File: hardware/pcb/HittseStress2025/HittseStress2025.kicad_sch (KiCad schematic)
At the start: 10 parts, among them J1 Conn_01x02_Socket, J2 Conn_01x02_Socket, J3 SMA_conector_female, U1 MINIDCDCBOOST5V, U2 TTGO_T-Beam_T22_V1.1

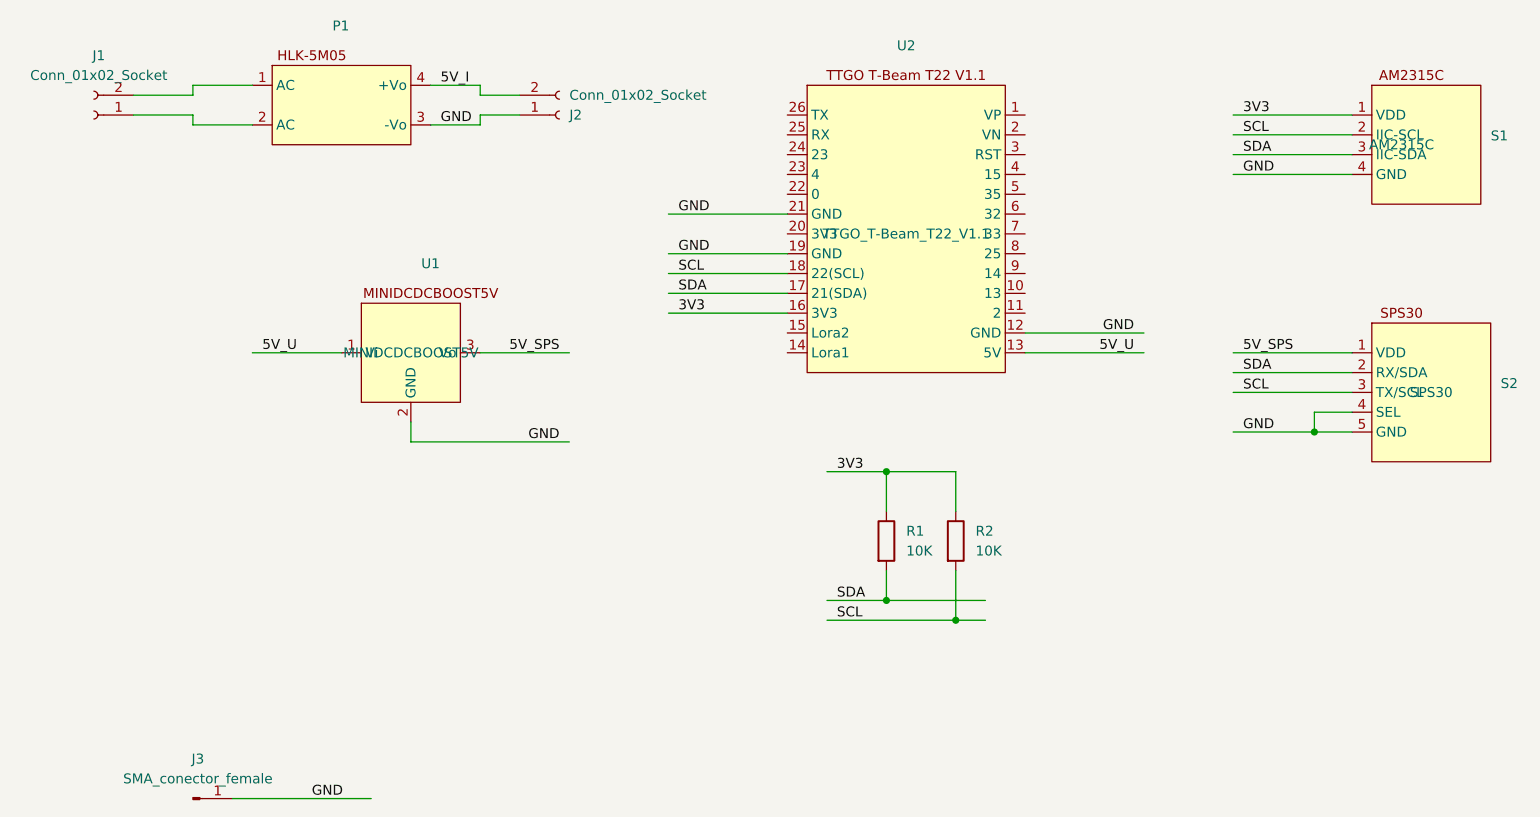
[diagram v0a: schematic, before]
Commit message: Updated to version 2025 for use with LilyGO T-Beam V1.2
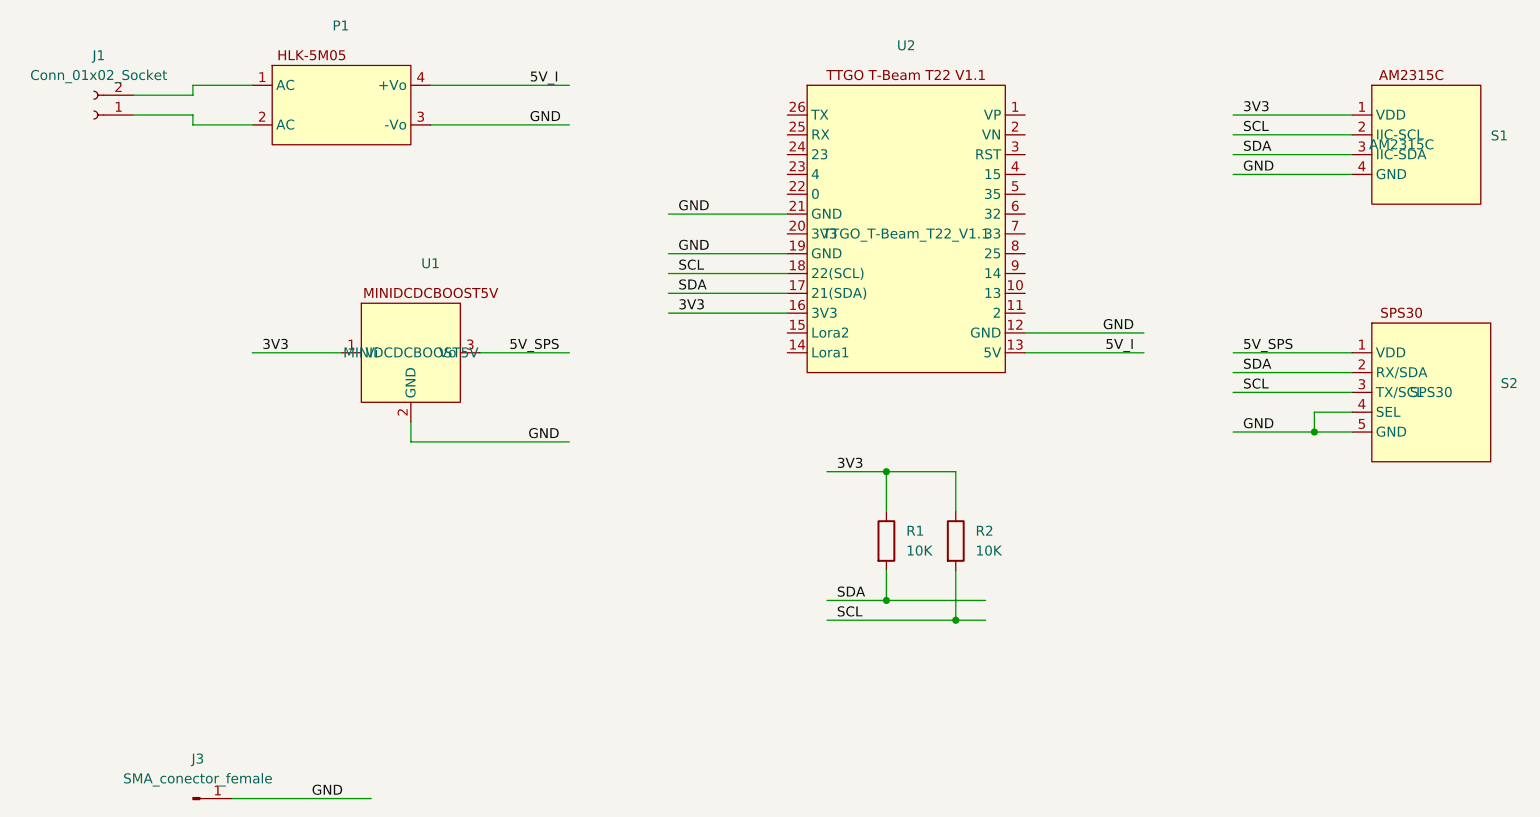
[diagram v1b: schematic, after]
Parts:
- removed J2: Conn_01x02_Socket, TerminalBlock_Phoenix:TerminalBlock_Phoenix_MPT-0,5-2-2.54_1x02_P2.54mm_Horizontal, symbol Connector:Conn_01x02_Socket
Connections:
- net 3V3: now also U1.1 (Vi)
- net 5V_I: now also U2.13 (5V)
- removed net 5V_U: U1.1 (Vi), U2.13 (5V)
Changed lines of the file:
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@@
-	(wire
-		(pts
-			(xy 81.28 64.77) (xy 81.28 66.04)
-		)
-		(stroke
-			(width 0)
-			(type default)
-		)
-	)
 	(wire
 		(pts
@@
 	(wire
 		(pts
-			(xy 81.28 60.96) (xy 81.28 62.23)
-		)
-		(stroke
-			(width 0)
-			(type default)
-		)
-	)
-	(wire
-		(pts
 			(xy 44.45 66.04) (xy 44.45 64.77)
 		)
@@
 	(wire
 		(pts
-			(xy 86.36 64.77) (xy 81.28 64.77)
-		)
-		(stroke
-			(width 0)
-			(type default)
-		)
-	)
-	(wire
-		(pts
 			(xy 125.73 129.54) (xy 142.24 129.54)
 		)
@@
 	(wire
 		(pts
-			(xy 81.28 62.23) (xy 86.36 62.23)
-		)
-		(stroke
-			(width 0)
-			(type default)
-		)
-	)
-	(wire
-		(pts
 			(xy 177.8 72.39) (xy 193.04 72.39)
 		)
@@
 	(wire
 		(pts
-			(xy 74.93 60.96) (xy 81.28 60.96)
+			(xy 74.93 60.96) (xy 92.71 60.96)
 		)
 		(stroke
@@
 	(wire
 		(pts
-			(xy 81.28 66.04) (xy 74.93 66.04)
-		)
-		(stroke
-			(width 0)
-			(type default)
-		)
-	)
-	(label "5V_U"
+			(xy 74.93 66.04) (xy 92.71 66.04)
+		)
+		(stroke
+			(width 0)
+			(type default)
+		)
+	)
+	(label "5V_I"
 		(at 165.1 95.25 180)
 		(effects
@@
 		)
 	)
-	(label "5V_U"
+	(label "3V3"
 		(at 53.34 95.25 0)
 		(effects
@@
 	)
 	(label "GND"
-		(at 76.2 66.04 0)
+		(at 87.63 66.04 0)
 		(effects
 			(font
@@
 	)
 	(label "5V_I"
-		(at 76.2 60.96 0)
+		(at 87.63 60.96 0)
 		(effects
 			(font
@@
 					(unit 1)
 				)
-			)
-		)
-	)
-	(symbol
-		(lib_id "Connector:Conn_01x02_Socket")
-		(at 91.44 64.77 0)
-		(mirror x)
-		(unit 1)
-		(exclude_from_sim no)
-		(in_bom yes)
-		(on_board yes)
-		(dnp no)
-		(property "Reference" "J2"
-			(at 92.71 64.77 0)
-			(effects
-				(font
-					(size 1.27 1.27)
-				)
-				(justify left)
-			)
-		)
-		(property "Value" "Conn_01x02_Socket"
-			(at 92.71 62.23 0)
-			(effects
-				(font
-					(size 1.27 1.27)
-				)
-				(justify left)
-			)
-		)
-		(property "Footprint" "TerminalBlock_Phoenix:TerminalBlock_Phoenix_MPT-0,5-2-2.54_1x02_P2.54mm_Horizontal"
-			(at 91.44 64.77 0)
-			(effects
-				(font
-					(size 1.27 1.27)
-				)
-				(hide yes)
-			)
-		)
-		(property "Datasheet" "~"
-			(at 91.44 64.77 0)
-			(effects
-				(font
-					(size 1.27 1.27)
-				)
-				(hide yes)
-			)
-		)
-		(property "Description" ""
-			(at 91.44 64.77 0)
-			(effects
-				(font
-					(size 1.27 1.27)
-				)
-			)
-		)
-		(pin "1"
-		)
-		(pin "2"
-		)
-		(instances
-			(project "HitteStress2023_pcb"
-				(path "/0b1ba7fb-a496-4717-8ed8-2a7de64e001c"
-					(reference "J2")
-					(unit 1)
-				)
